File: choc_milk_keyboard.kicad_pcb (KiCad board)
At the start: 2 copper layers, 20 x 38 mm, 6 parts, among them J1 Conn_01x02_Female, SW1 SW_PUSH, SW2 SW_PUSH, U1 ProMicro

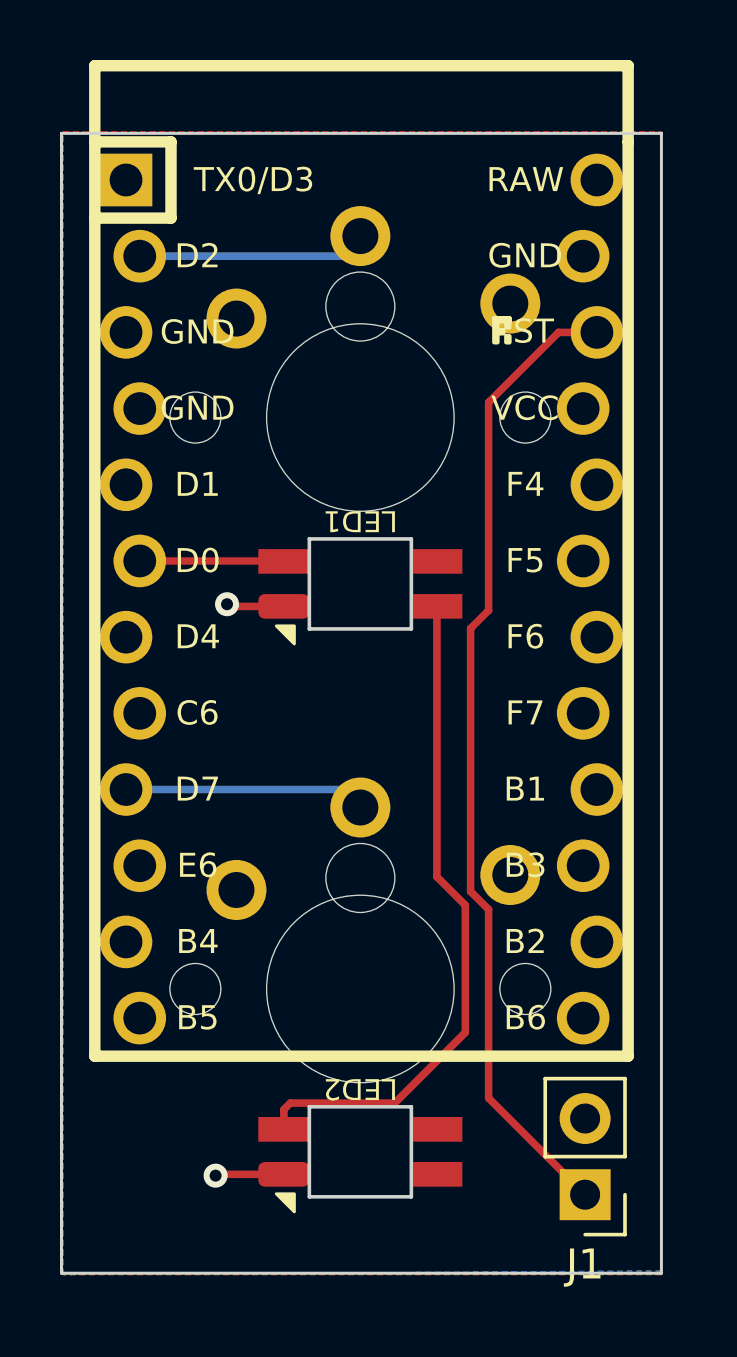
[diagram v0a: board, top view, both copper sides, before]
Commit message: Refactored for USB-C ProMicro USB-C is 3mm longer than micro usb Created a new footprint variant
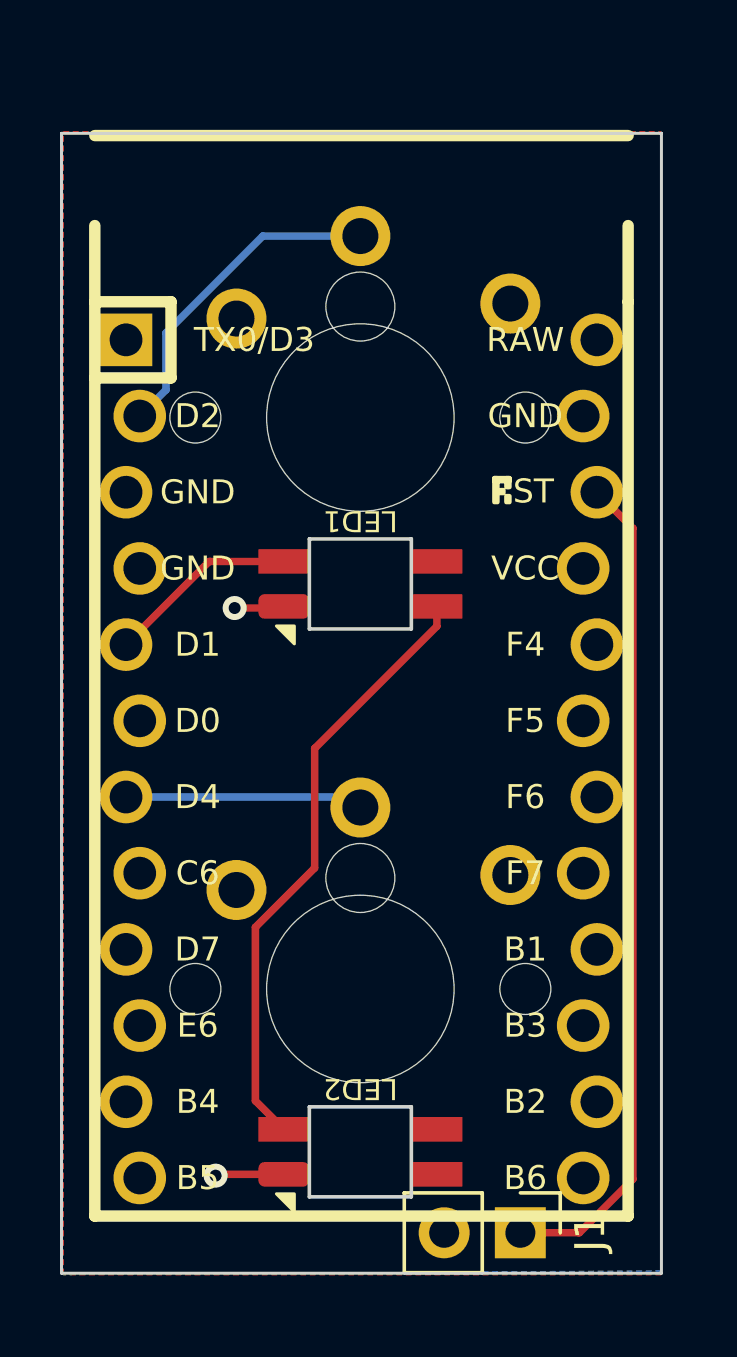
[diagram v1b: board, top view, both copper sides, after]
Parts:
- U1: footprint Keebio-Parts:ArduinoProMicro-ZigZag -> ergodonk_kicad_library:ArduinoProMicro-ZigZag-USB-C_hidden_text
- moved U1 5.33 mm to (85.0, 120.9)
- moved J1 2.50 mm to (90.3, 136.7), turned to -90 degrees
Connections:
- LED1 pad 4: Net-(U1-Pad6) -> Net-(U1-Pad5)
- SW2 pad 1: Net-(SW2-Pad1) -> Net-(U1-Pad7)
- U1 pad 3: unconnected-(U1-Pad3) -> GND
- U1 pad 4: unconnected-(U1-Pad4) -> GND
- U1 pad 5: unconnected-(U1-Pad5) -> Net-(U1-Pad5)
- U1 pad 6: Net-(U1-Pad6) -> unconnected-(U1-Pad6)
- U1 pad 7: unconnected-(U1-Pad7) -> Net-(U1-Pad7)
- U1 pad 9: Net-(SW2-Pad1) -> unconnected-(U1-Pad9)
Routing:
- net Net-(SW2-Pad1): track 8.06 -> 0.00 mm
- net Net-(U1-Pad7): track 0.00 -> 7.96 mm
- net Net-(U1-Pad5): track 0.00 -> 6.41 mm
- net Net-(J1-Pad1): track 32.8 -> 27.9 mm
- net Net-(U1-Pad6): track 4.91 -> 0.00 mm
- net Net-(SW1-Pad1): track 7.63 -> 11.0 mm
- net Net-(LED1-Pad2): track 22.4 -> 20.3 mm
- net GND: track 4.63 -> 3.96 mm
- net unconnected-(U1-Pad8): track 0.65 -> 0.00 mm

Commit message: Added 3d models, flipped pro micro
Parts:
- SW1, SW2: footprint ergodonk_kicad_library:Low-Profile-Choc-MX -> ergodonk_kicad_library:Low-Profile-Choc-MX_no_text
- U1: moved to B.Cu
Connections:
- LED1 pad 4: Net-(U1-Pad5) -> unconnected-(LED1-Pad4)
- U1 pad 20: unconnected-(U1-Pad20) -> unconnected-(LED1-Pad4)
- U1 pad 5: Net-(U1-Pad5) -> unconnected-(U1-Pad5)
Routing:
- net Net-(J1-Pad1): track 27.9 -> 39.5 mm
- net unconnected-(LED1-Pad4): track 0.00 -> 6.54 mm
- net Net-(U1-Pad5): track 6.41 -> 0.00 mm
- net Net-(SW1-Pad1): track 11.0 -> 9.91 mm

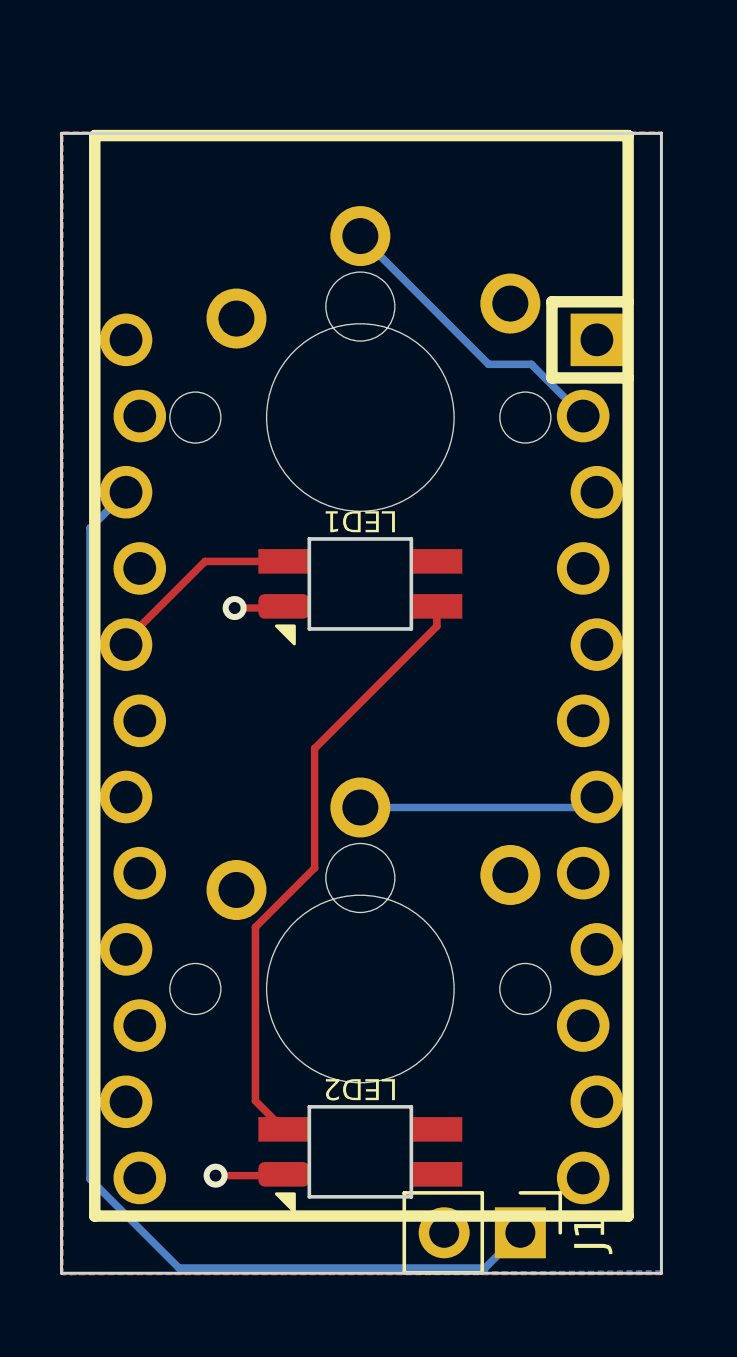
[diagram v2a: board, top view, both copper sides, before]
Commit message: Revised Choc footprint and added logo There are 2 Choc V2 variants - one has an extra non-functional pin. Added drawings and added hole to footprint. Flipped switches and Leds to make routing around hole cleaner Added multilayer logo
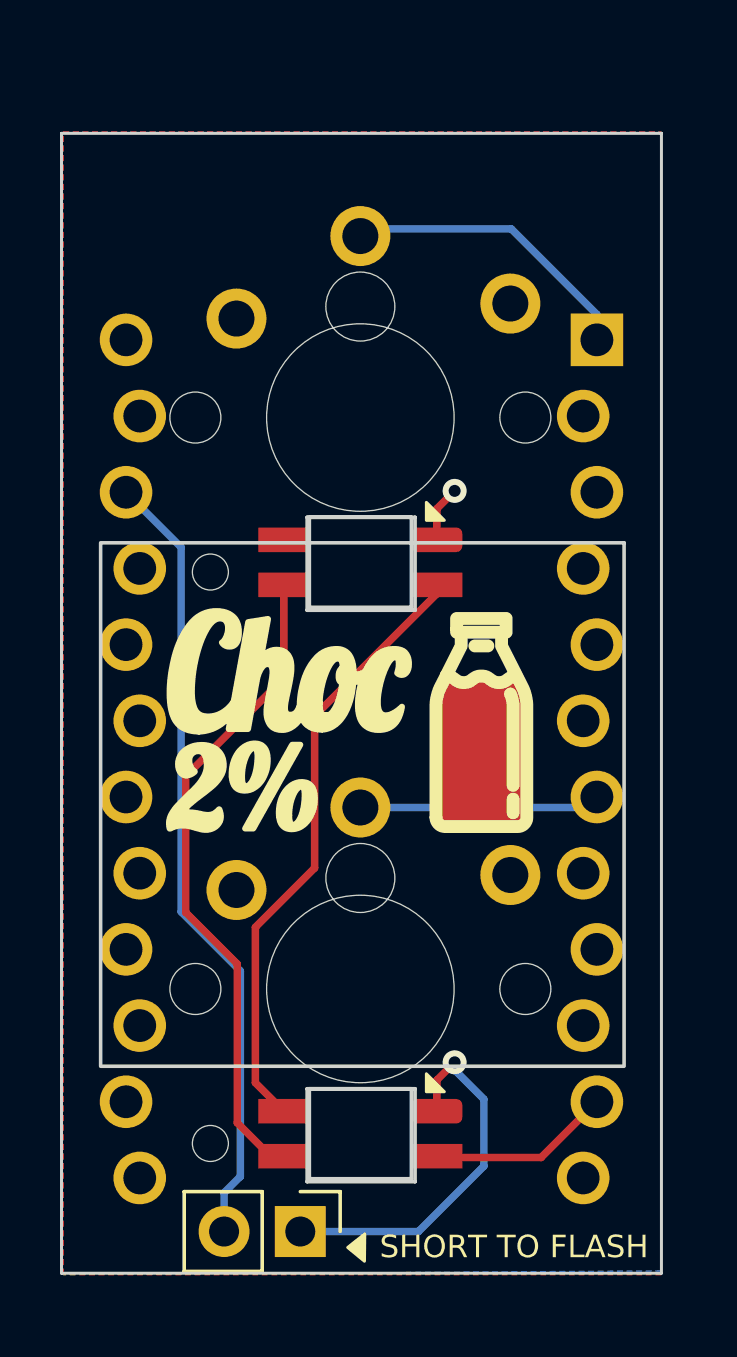
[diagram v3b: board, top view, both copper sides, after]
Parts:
- added REF**: Milk_gold_logo, ergodonk_kicad_library:Milk_gold_logo, F.Cu at (89.0, 119.7)
- moved LED2 19.7 mm to (85.0, 114.3), turned to 0 degrees
- moved SW1 19.0 mm to (85.0, 128.5)
- moved SW2 19.0 mm to (85.0, 109.5)
- moved LED1 18.3 mm to (85.0, 133.3), turned to 0 degrees
- moved J1 7.34 mm to (83.0, 136.6)
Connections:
- J1 pad 1: Net-(J1-Pad1) -> GND
- J1 pad 2: GND -> Net-(U1-Pad22)
- LED1 pad 4: unconnected-(LED1-Pad4) -> Net-(U1-Pad11)
- SW2 pad 1: Net-(SW2-Pad1) -> Net-(U1-Pad1)
- U1 pad 1: unconnected-(U1-Pad1) -> Net-(U1-Pad1)
- U1 pad 11: unconnected-(U1-Pad11) -> Net-(U1-Pad11)
- U1 pad 2: Net-(SW1-Pad1) -> unconnected-(U1-Pad2)
- U1 pad 20: unconnected-(LED1-Pad4) -> unconnected-(U1-Pad20)
- U1 pad 22: Net-(J1-Pad1) -> Net-(U1-Pad22)
- U1 pad 7: Net-(SW2-Pad1) -> Net-(SW1-Pad1)
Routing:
- net Net-(J1-Pad1): track 39.5 -> 0.00 mm
- net Net-(U1-Pad22): track 0.00 -> 26.4 mm
- net VCC: track 0.00 -> 22.7 mm
- net GND: track 3.96 -> 14.4 mm
- net Net-(U1-Pad1): track 0.00 -> 10.2 mm
- net Net-(SW2-Pad1): track 8.03 -> 0.00 mm
- net unconnected-(LED1-Pad4): track 6.54 -> 0.00 mm
- net Net-(U1-Pad11): track 0.00 -> 6.12 mm
- net Net-(SW1-Pad1): track 9.91 -> 8.03 mm
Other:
- board text added: "SHORT TO FLASH"

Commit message: Logo tweak for production and added todo list
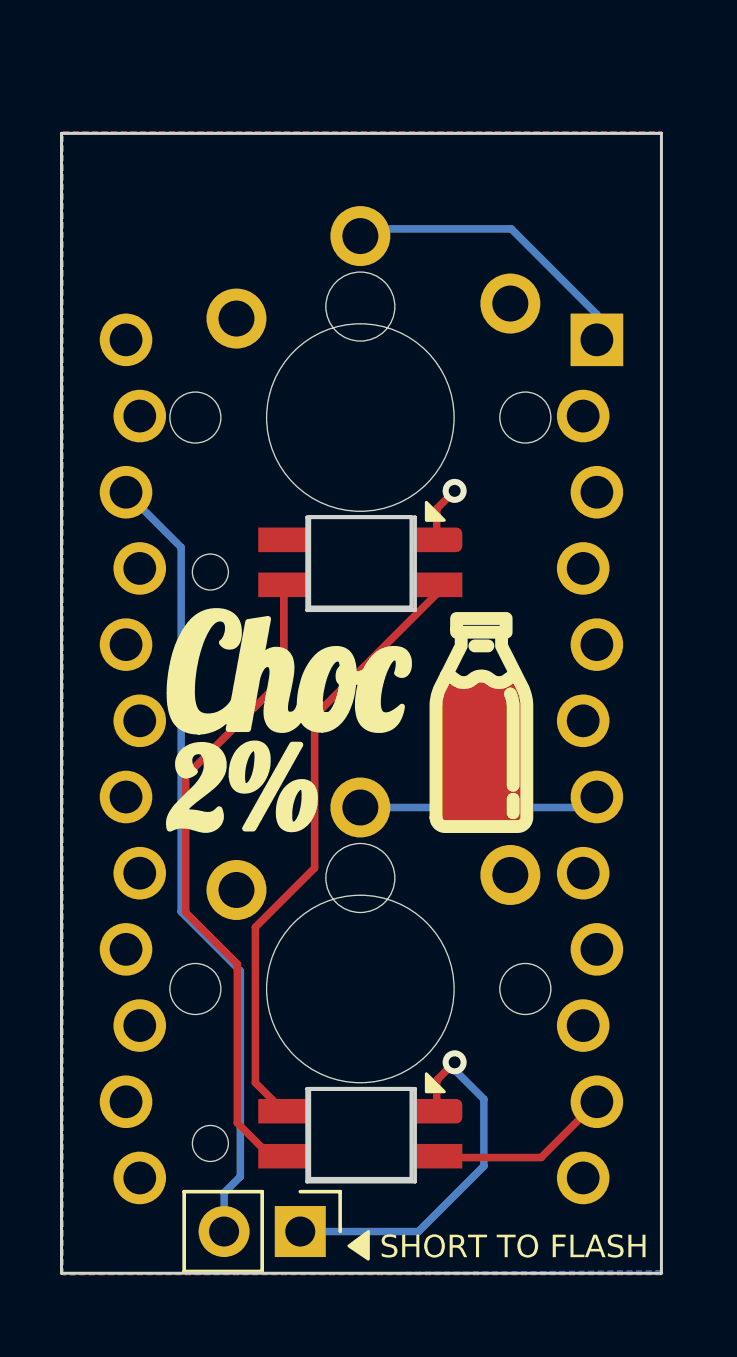
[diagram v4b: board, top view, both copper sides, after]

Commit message: Logo rework, rewire to use classic firmware, silkscreeen tidy
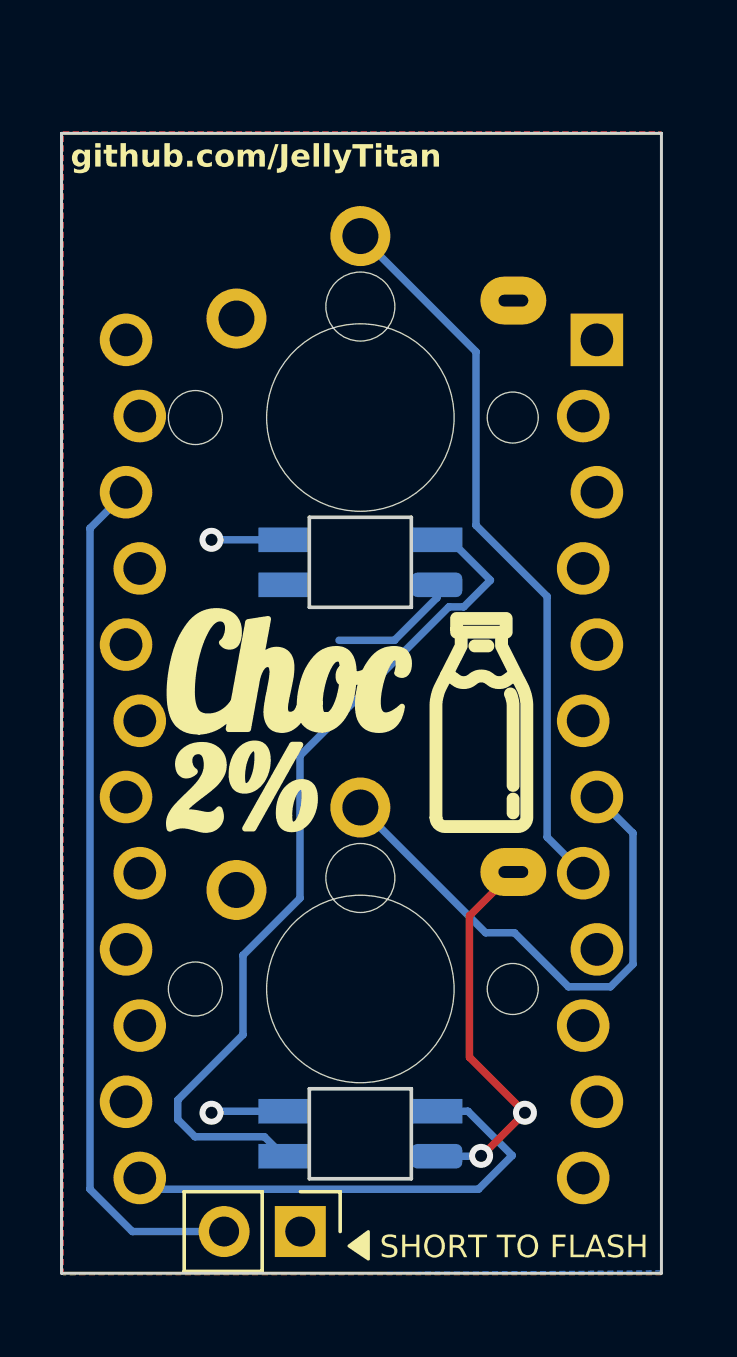
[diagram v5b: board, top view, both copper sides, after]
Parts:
- LED1, LED2: moved to B.Cu
- REF**: value Milk_gold_logo -> Milk_gold_logo_V2; footprint ergodonk_kicad_library:Milk_gold_logo -> ergodonk_kicad_library:Milk_gold_logo_V2
- SW1, SW2: footprint ergodonk_kicad_library:Low-Profile-Choc-MX_no_text -> ergodonk_kicad_library:Low-Profile-Choc-MX_no_text_V2
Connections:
- LED1 pad 4: Net-(U1-Pad11) -> Net-(LED1-DIN)
- SW2 pad 1: Net-(U1-Pad1) -> Net-(U1-5/C6)
- U1 pad 1: Net-(U1-Pad1) -> unconnected-(U1-TX0/D3-Pad1)
- U1 pad 11: Net-(U1-Pad11) -> unconnected-(U1-8/B4-Pad11)
- U1 pad 13: unconnected-(U1-Pad13) -> Net-(LED1-DIN)
- U1 pad 8: unconnected-(U1-Pad8) -> Net-(U1-5/C6)
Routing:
- net Net-(U1-5/C6): track 0.00 -> 24.3 mm
- net VCC: track 22.7 -> 4.85 mm, vias 0 -> 2
- net Net-(LED1-DIN): track 0.00 -> 16.2 mm
- net Net-(U1-4/D4): track 8.03 -> 18.4 mm
- net Net-(U1-Pad1): track 10.2 -> 0.00 mm
- net Net-(LED1-DOUT): track 20.4 -> 29.0 mm
- net Net-(U1-Pad11): track 6.12 -> 0.00 mm
- net GND: track 14.4 -> 17.2 mm
- net Net-(J1-Pin_2): track 26.4 -> 28.8 mm
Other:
- board text added: "github.com/JellyTitan"

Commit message: Moved footprints to new library Sent this version out for production Added tweezer holes to LEDs Cleaned up microcontroller footprint
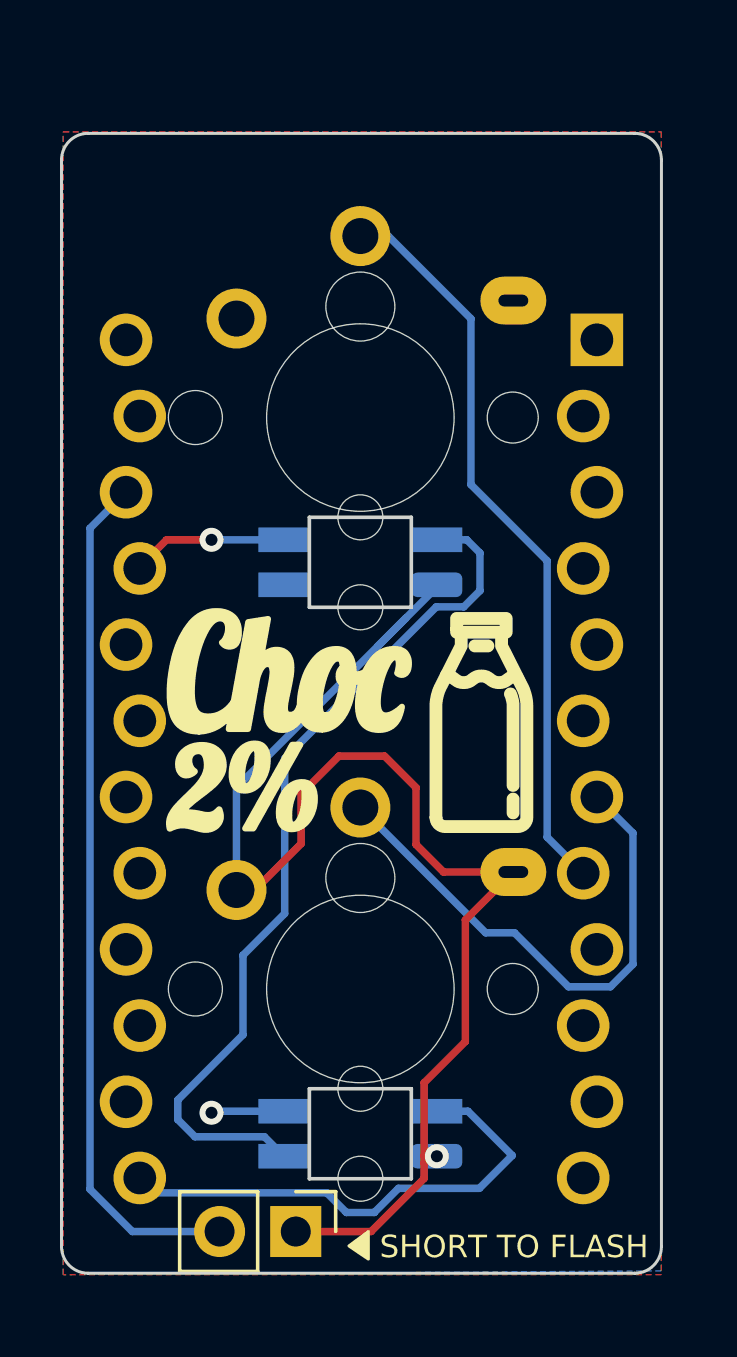
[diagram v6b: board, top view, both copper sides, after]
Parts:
- LED1, LED2: footprint Keebio-Parts:SK6812-MINI-E -> Choc-milk-parts:SK6812-MINI-E
- REF**: footprint ergodonk_kicad_library:Milk_gold_logo_V2 -> Choc-milk-parts:Milk_gold_logo_V2
- SW1, SW2: footprint ergodonk_kicad_library:Low-Profile-Choc-MX_no_text_V2 -> Choc-milk-parts:Low-Profile-MX-Choc-V1-V2
- U1: footprint ergodonk_kicad_library:ArduinoProMicro-ZigZag-USB-C_hidden_text -> Choc-milk-parts:ArduinoProMicro-ZigZag-USB-C_hidden_text
- moved J1 0.15 mm to (82.8, 136.6)
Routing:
- net GND: track 17.2 -> 46.5 mm, vias 2 -> 1
- net VCC: track 4.85 -> 7.67 mm
- net Net-(LED1-DIN): track 16.2 -> 16.8 mm
- net Net-(U1-5/C6): track 24.3 -> 24.9 mm
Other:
- outline, holes or cut-outs redrawn
